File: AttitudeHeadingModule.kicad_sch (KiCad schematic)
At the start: 11 parts, among them J2 Conn_01x04, U2 ICM-20948, U3 MMC5603NJ, U4 SN74AVC4T774PW

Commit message: Change IMU to ISM330DHCX and remove SPI level converter
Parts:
- removed C16, C17, C18: 100nF, symbol Device:C
- removed U2: ICM-20948, Sensor_Motion:InvenSense_QFN-24_3x3mm_P0.4mm, symbol Sensor_Motion:ICM-20948
- removed U4: SN74AVC4T774PW, PW16, symbol XuLab:SN74AVC4T774PW
- added U2: ISM330DHCX, Package_LGA:LGA-14_3x2.5mm_P0.5mm_LayoutBorder3x4y, symbol Sensor_Motion:ISM330DHCX
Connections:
- net +1V8 is gone; now on net +3V3: C15.1
- net +3V3: now also U2.5 (VDDIO), U2.8 (VDD)
- net GND: now also U2.2 (SDx), U2.3 (SCx), U2.6 (GND), U2.7 (GND)
- net SPI1_CS1: now also U2.12 (CS)
- net SPI1_MISO: now also U2.1 (SDO/SA0)
- net SPI1_MOSI: now also U2.14 (SDA)
- net SPI1_SCK: now also U2.13 (SCL)
- no-connect marks 3 -> 4

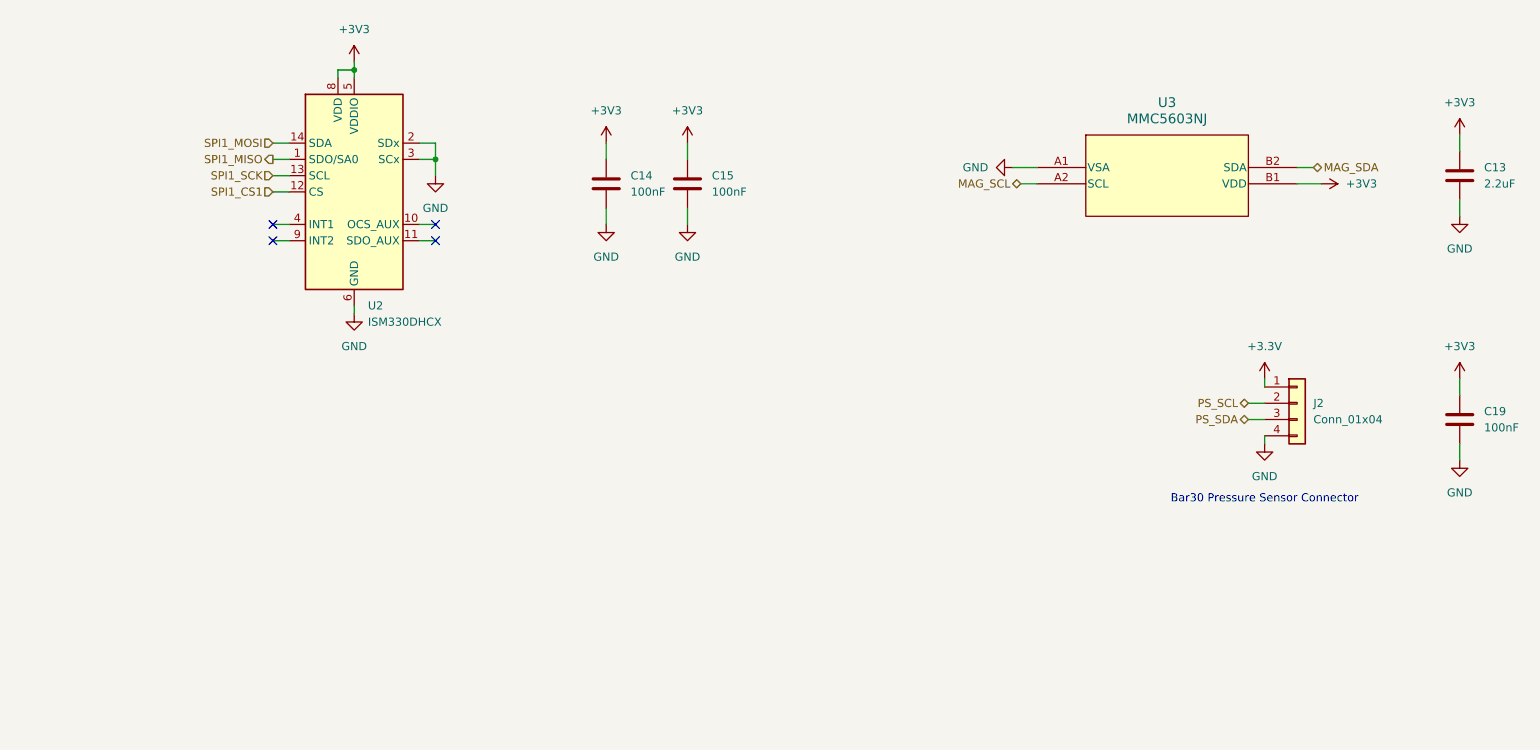
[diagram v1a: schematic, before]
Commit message: Change magnetometer to MMC5983MA
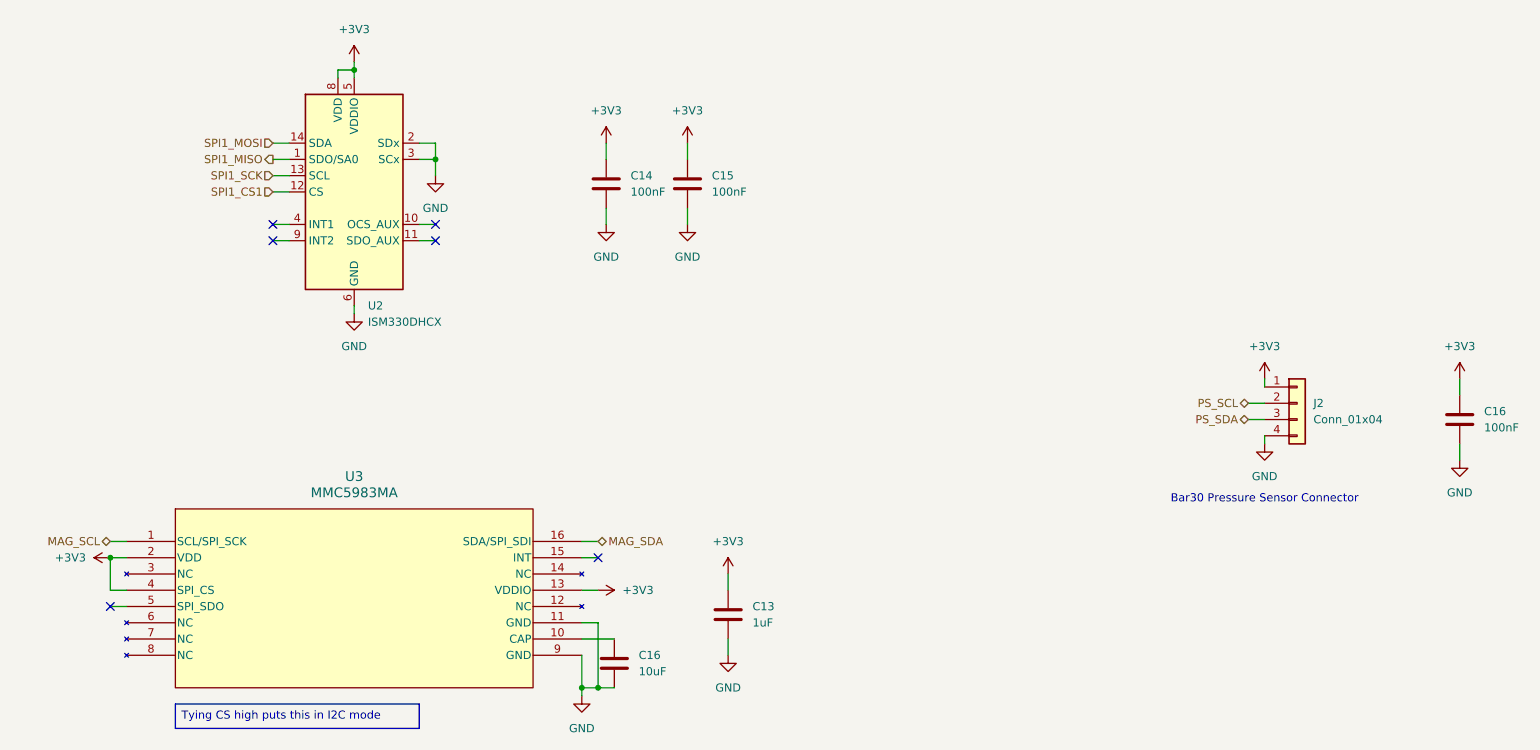
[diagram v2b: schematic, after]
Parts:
- removed U3: MMC5603NJ, Package_BGA:WLP-4_0.82X0.82mm_MEM, symbol XuLab:MMC5603NJ
- added C16: 10uF, symbol Device:C
- added U3: MMC5983MA, MMC5983MA_MEM, symbol XuLab:MMC5983MA
- C13: value 2.2uF -> 1uF
- renumbered C19 to C16
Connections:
- net +3.3V is gone; now on net +3V3: J2.1 (Pin_1)
- net +3V3: now also U3.13 (VDDIO), U3.2 (VDD), U3.4 (SPI_CS)
- net GND: now also C16.2, U3.11 (GND), U3.9 (GND)
- net MAG_SCL: now also U3.1 (SCL/SPI_SCK)
- net MAG_SDA: now also U3.16 (SDA/SPI_SDI)
- new net: C16.1, U3.10 (CAP)
- no-connect marks 4 -> 6
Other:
- moved on the sheet: C13

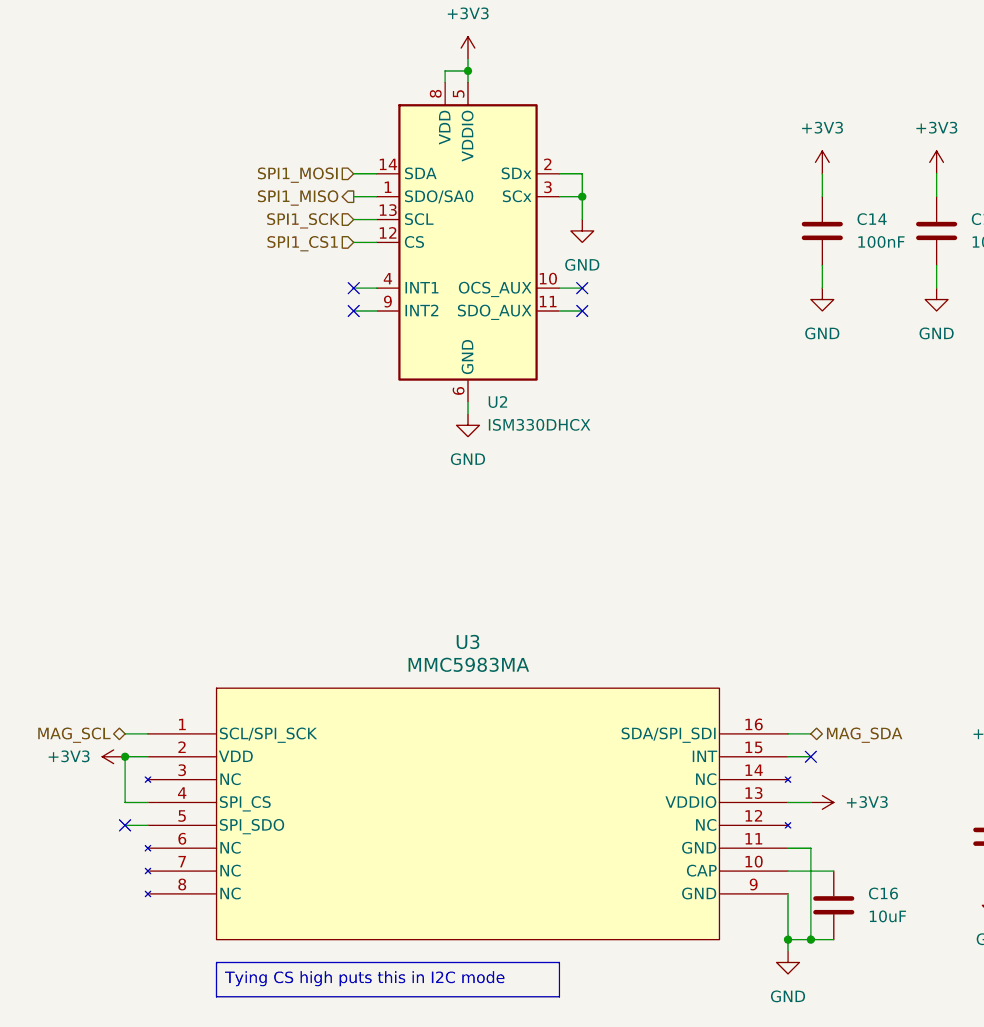
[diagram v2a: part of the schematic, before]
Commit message: Change magnetometer interface from I2C to SPI
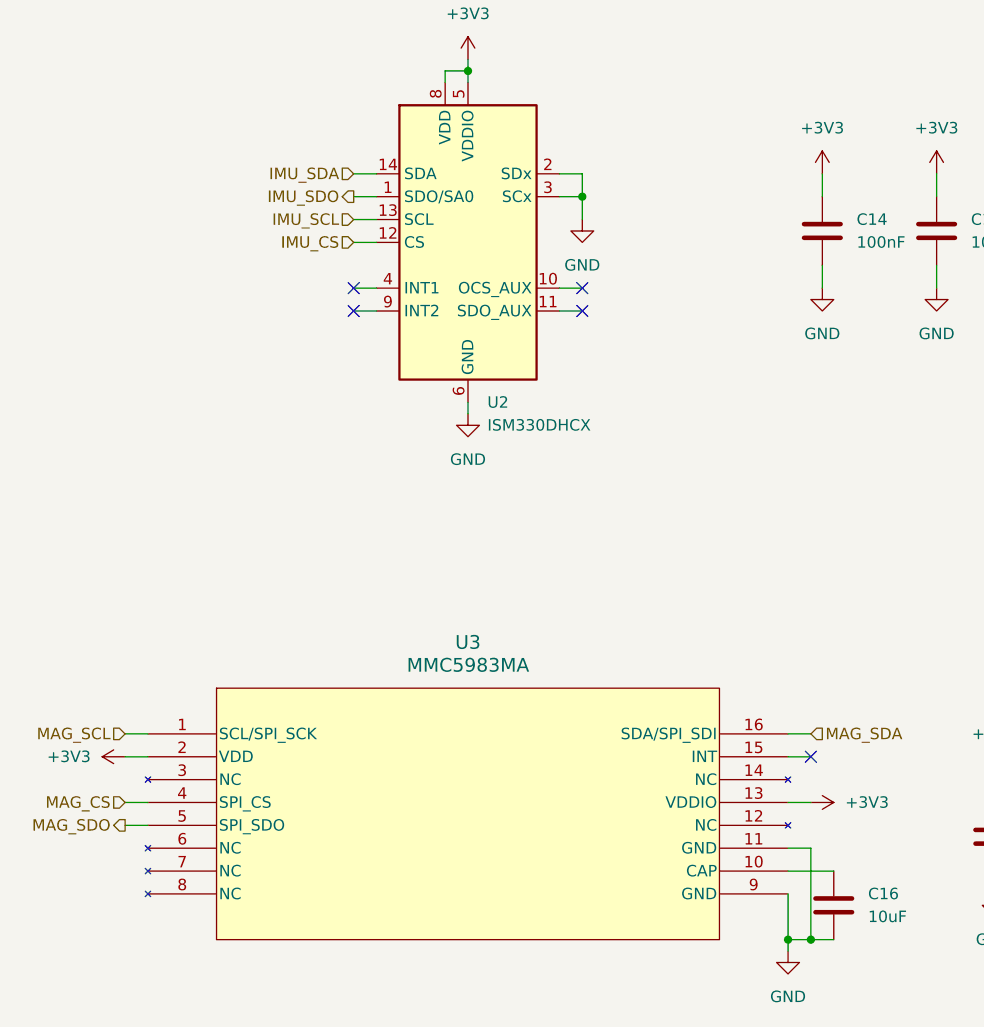
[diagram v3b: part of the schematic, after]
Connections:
- net +3V3: no longer U3.4 (SPI_CS)
- net MAG_SDO: now reaches U3.5 (SPI_SDO)
- net SPI1_CS1 renamed IMU_CS
- net SPI1_MISO renamed IMU_SDO
- net SPI1_MOSI renamed IMU_SDA
- net SPI1_SCK renamed IMU_SCL
- new net MAG_CS: U3.4 (SPI_CS)
- no-connect marks 6 -> 5
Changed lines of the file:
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@@
-		)
-	)
-	(text_box "Tying CS high puts this in I2C mode"
-		(exclude_from_sim no)
-		(at 53.34 133.35 0)
-		(size 38.1 3.81)
-		(margins 0.9525 0.9525 0.9525 0.9525)
-		(stroke
-			(width 0)
-			(type solid)
-		)
-		(fill
-			(type none)
-		)
-		(effects
-			(font
-				(size 1.27 1.27)
-			)
-			(justify left top)
 		)
 	)
@@
 	)
 	(junction
-		(at 43.18 110.49)
-		(diameter 0)
-		(color 0 0 0 0)
-	)
-	(junction
 		(at 93.98 48.26)
 		(diameter 0)
@@
 	)
 	(no_connect
-		(at 43.18 118.11)
-	)
-	(no_connect
 		(at 68.58 58.42)
 	)
@@
 	(wire
 		(pts
-			(xy 43.18 110.49) (xy 43.18 115.57)
-		)
-		(stroke
-			(width 0)
-			(type default)
-		)
-	)
-	(wire
-		(pts
 			(xy 116.84 107.95) (xy 119.38 107.95)
 		)
@@
 		)
 	)
-	(hierarchical_label "SPI1_CS1"
+	(hierarchical_label "MAG_SDO"
+		(shape output)
+		(at 43.18 118.11 180)
+		(effects
+			(font
+				(size 1.27 1.27)
+			)
+			(justify right)
+		)
+	)
+	(hierarchical_label "IMU_CS"
 		(shape input)
 		(at 68.58 53.34 180)
@@
 	)
 	(hierarchical_label "MAG_SDA"
-		(shape bidirectional)
+		(shape input)
 		(at 119.38 107.95 0)
 		(effects
@@
 		)
 	)
-	(hierarchical_label "SPI1_SCK"
+	(hierarchical_label "IMU_SCL"
 		(shape input)
 		(at 68.58 50.8 180)
@@
 		)
 	)
-	(hierarchical_label "SPI1_MOSI"
+	(hierarchical_label "IMU_SDA"
 		(shape input)
 		(at 68.58 45.72 180)
@@
 		)
 	)
-	(hierarchical_label "SPI1_MISO"
+	(hierarchical_label "IMU_SDO"
 		(shape output)
 		(at 68.58 48.26 180)
@@
 	)
 	(hierarchical_label "MAG_SCL"
-		(shape bidirectional)
+		(shape input)
 		(at 43.18 107.95 180)
 		(effects
 			(font
+				(size 1.27 1.27)
+			)
+			(justify right)
+		)
+	)
+	(hierarchical_label "MAG_CS"
+		(shape input)
+		(at 43.18 115.57 180)
+		(effects
+			(font

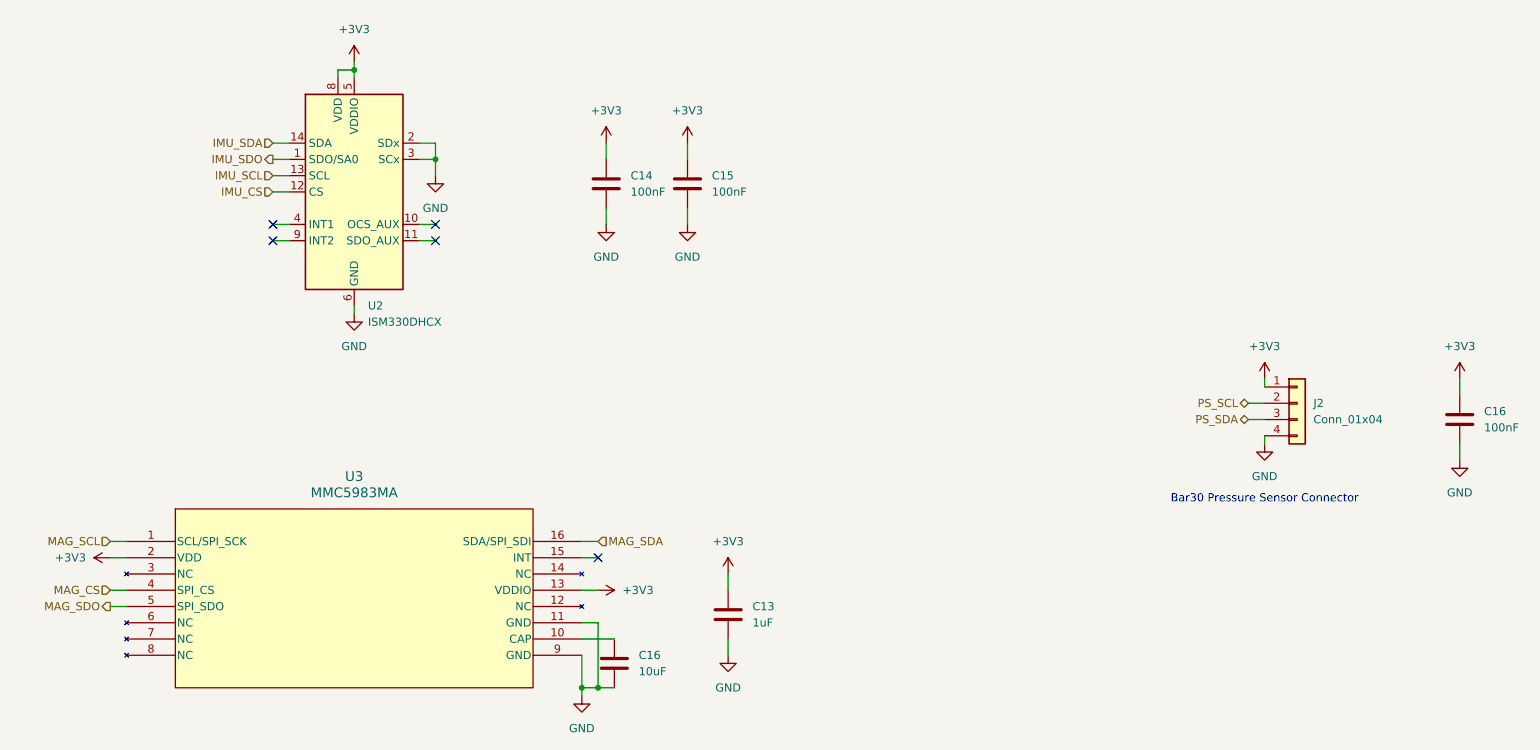
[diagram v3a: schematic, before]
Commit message: Fix duplicate capacitor labels
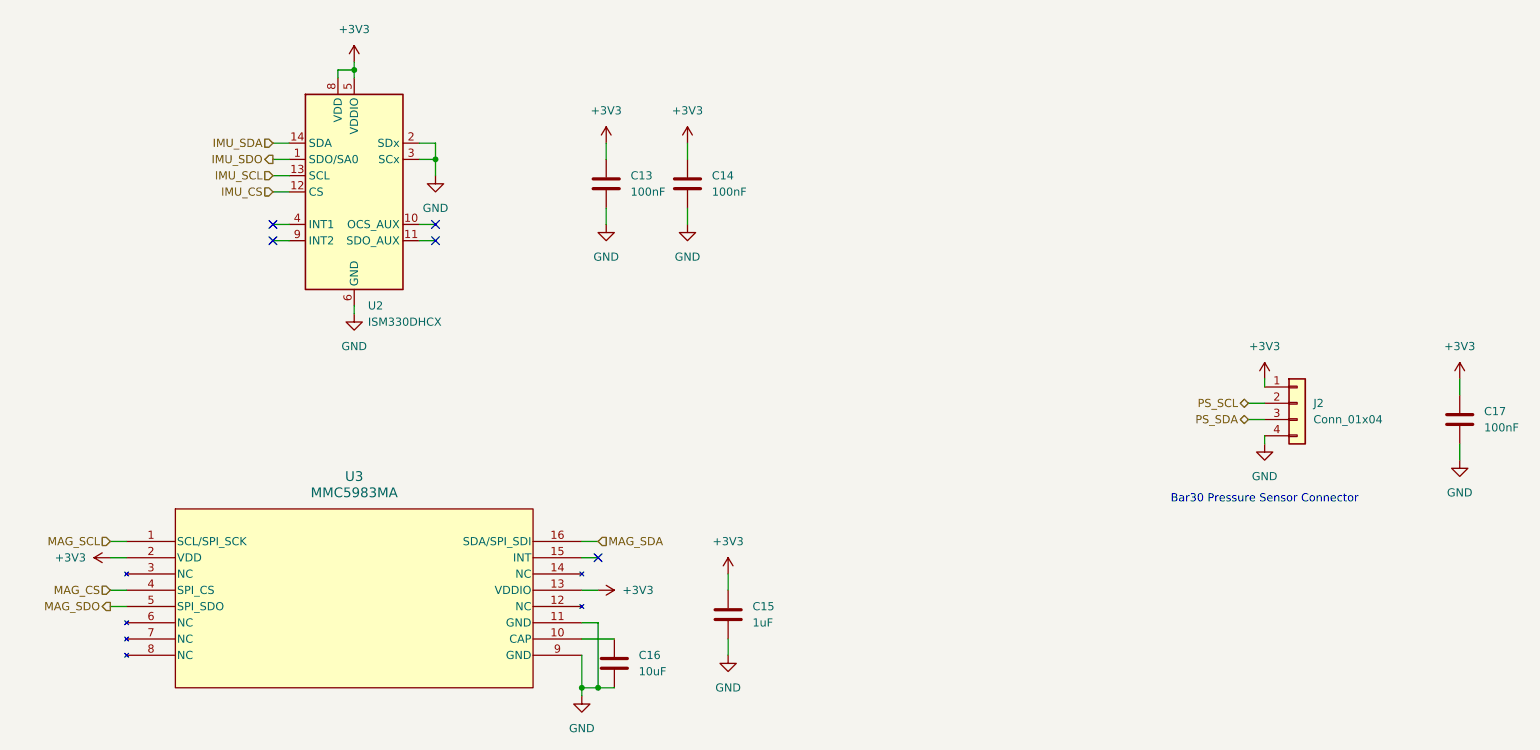
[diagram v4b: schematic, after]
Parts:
- renumbered C14 to C13, C15 to C14, C13 to C15, C16 to C17
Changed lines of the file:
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@@
 		(dnp no)
 		(fields_autoplaced yes)
-		(property "Reference" "C13"
+		(property "Reference" "C15"
 			(at 143.51 118.1099 0)
 			(effects
@@
 			(project "XuLabPlatform"
 				(path "/71bb14ae-b730-4d22-a41d-cf68989dae2d/a5713b00-422c-456a-9938-13721b057665"
-					(reference "C13")
+					(reference "C15")
 					(unit 1)
 				)
@@
 		(dnp no)
 		(fields_autoplaced yes)
-		(property "Reference" "C14"
+		(property "Reference" "C13"
 			(at 124.46 50.7999 0)
 			(effects
@@
 			(project "XuLabPlatform"
 				(path "/71bb14ae-b730-4d22-a41d-cf68989dae2d/a5713b00-422c-456a-9938-13721b057665"
-					(reference "C14")
+					(reference "C13")
 					(unit 1)
 				)
@@
 		(dnp no)
 		(fields_autoplaced yes)
-		(property "Reference" "C16"
+		(property "Reference" "C17"
 			(at 257.81 87.6299 0)
 			(effects
@@
 			(project "XuLabPlatform"
 				(path "/71bb14ae-b730-4d22-a41d-cf68989dae2d/a5713b00-422c-456a-9938-13721b057665"
-					(reference "C16")
+					(reference "C17")
 					(unit 1)
 				)
@@
 		(dnp no)
 		(fields_autoplaced yes)
-		(property "Reference" "C15"
+		(property "Reference" "C14"
 			(at 137.16 50.7999 0)
 			(effects
@@
 			(project "XuLabPlatform"
 				(path "/71bb14ae-b730-4d22-a41d-cf68989dae2d/a5713b00-422c-456a-9938-13721b057665"
-					(reference "C15")
-					(unit 1)
-				)
+					(reference "C14")
+					(unit 1)
+				)
